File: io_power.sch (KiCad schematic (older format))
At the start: 30 parts, among them J7 Conn_02x03_Odd_Even, U11 TPS7A7100, U12 TPS7A7100, U13 ADS1115IDGS, U5 TCA6424A, U6 TPS7A7100

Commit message: sch: List LCSC P/N for each component
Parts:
- C22, C23, C24, C25, C26, C27, C31, C32, C33: LCSC P/N (none) -> C1591; MFR P/N (none) -> CL10B104KB8NNNC
- C28, C29, C30: LCSC P/N (none) -> C19702; MFR P/N (none) -> CL10A106KP8NNNC
- J7: LCSC P/N (none) -> C65114; MFR P/N (none) -> C65114
- R21, R22, R23: LCSC P/N (none) -> C115324; MFR P/N (none) -> RS-03K1002FT
- R24, R25, R26: LCSC P/N (none) -> C327826; MFR P/N (none) -> MR06X1003FTL
- R27, R28, R29: LCSC P/N (none) -> C413703; MFR P/N (none) -> ERJPB3B3002V
- R30, R31, R32: LCSC P/N (none) -> C191225; MFR P/N (none) -> ERJPB3B2002V
- U11, U12, U6: LCSC P/N (none) -> C129327; MFR P/N (none) -> TPS7A7100RGTR
- U13: LCSC P/N (none) -> C37593; MFR P/N (none) -> ADS1115IDGSR
- U5: LCSC P/N (none) -> C80692; MFR P/N (none) -> TCA6424ARGJR
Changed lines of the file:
@@
 F 2 "antboard:VQFN-16-1EP_3x3mm_P0.5mm_EP1.6x1.6mm_ThermalVias" H 7650 1100 50  0001 C CNN
 F 3 "https://www.ti.com/lit/ds/symlink/tps7a7100.pdf" H 7650 1100 50  0001 C CNN
+F 4 "C129327" H 7650 1100 50  0001 C CNN "LCSC P/N"
+F 5 "TPS7A7100RGTR" H 7650 1100 50  0001 C CNN "MFR P/N"
 	1    7650 1100
 	1    0    0    -1
@@
 F 2 "Capacitor_SMD:C_0603_1608Metric" H 8650 1400 50  0001 C CNN
 F 3 "~" H 8650 1400 50  0001 C CNN
+F 4 "C1591" H 8650 1400 50  0001 C CNN "LCSC P/N"
+F 5 "CL10B104KB8NNNC" H 8650 1400 50  0001 C CNN "MFR P/N"
 	1    8650 1400
 	-1   0    0    -1
@@
 F 2 "Resistor_SMD:R_0603_1608Metric" H 9000 1650 50  0001 C CNN
 F 3 "~" H 9000 1650 50  0001 C CNN
+F 4 "C327826" H 9000 1650 50  0001 C CNN "LCSC P/N"
+F 5 "MR06X1003FTL" H 9000 1650 50  0001 C CNN "MFR P/N"
 	1    9000 1650
 	1    0    0    -1
@@
 F 2 "antboard:VQFN-16-1EP_3x3mm_P0.5mm_EP1.6x1.6mm_ThermalVias" H 7650 2850 50  0001 C CNN
 F 3 "https://www.ti.com/lit/ds/symlink/tps7a7100.pdf" H 7650 2850 50  0001 C CNN
+F 4 "C129327" H 7650 2850 50  0001 C CNN "LCSC P/N"
+F 5 "TPS7A7100RGTR" H 7650 2850 50  0001 C CNN "MFR P/N"
 	1    7650 2850
 	1    0    0    -1
@@
 F 2 "Capacitor_SMD:C_0603_1608Metric" H 8650 3150 50  0001 C CNN
 F 3 "~" H 8650 3150 50  0001 C CNN
+F 4 "C1591" H 8650 3150 50  0001 C CNN "LCSC P/N"
+F 5 "CL10B104KB8NNNC" H 8650 3150 50  0001 C CNN "MFR P/N"
 	1    8650 3150
 	-1   0    0    -1
@@
 F 2 "Resistor_SMD:R_0603_1608Metric" H 9000 3400 50  0001 C CNN
 F 3 "~" H 9000 3400 50  0001 C CNN
+F 4 "C327826" H 9000 3400 50  0001 C CNN "LCSC P/N"
+F 5 "MR06X1003FTL" H 9000 3400 50  0001 C CNN "MFR P/N"
 	1    9000 3400
 	1    0    0    -1
@@
 F 2 "antboard:VQFN-16-1EP_3x3mm_P0.5mm_EP1.6x1.6mm_ThermalVias" H 7650 4600 50  0001 C CNN
 F 3 "https://www.ti.com/lit/ds/symlink/tps7a7100.pdf" H 7650 4600 50  0001 C CNN
+F 4 "C129327" H 7650 4600 50  0001 C CNN "LCSC P/N"
+F 5 "TPS7A7100RGTR" H 7650 4600 50  0001 C CNN "MFR P/N"
 	1    7650 4600
 	1    0    0    -1
@@
 F 2 "Capacitor_SMD:C_0603_1608Metric" H 8650 4900 50  0001 C CNN
 F 3 "~" H 8650 4900 50  0001 C CNN
+F 4 "C1591" H 8650 4900 50  0001 C CNN "LCSC P/N"
+F 5 "CL10B104KB8NNNC" H 8650 4900 50  0001 C CNN "MFR P/N"
 	1    8650 4900
 	-1   0    0    -1
@@
 F 2 "Resistor_SMD:R_0603_1608Metric" H 9000 5150 50  0001 C CNN
 F 3 "~" H 9000 5150 50  0001 C CNN
+F 4 "C327826" H 9000 5150 50  0001 C CNN "LCSC P/N"
+F 5 "MR06X1003FTL" H 9000 5150 50  0001 C CNN "MFR P/N"
 	1    9000 5150
 	1    0    0    -1
@@
 F 2 "Capacitor_SMD:C_0603_1608Metric" H 7350 5700 50  0001 C CNN
 F 3 "~" H 7350 5700 50  0001 C CNN
+F 4 "C1591" H 7350 5700 50  0001 C CNN "LCSC P/N"
+F 5 "CL10B104KB8NNNC" H 7350 5700 50  0001 C CNN "MFR P/N"
 	1    7350 5700
 	-1   0    0    -1
@@
 F 2 "Capacitor_SMD:C_0603_1608Metric" H 7350 3950 50  0001 C CNN
 F 3 "~" H 7350 3950 50  0001 C CNN
+F 4 "C1591" H 7350 3950 50  0001 C CNN "LCSC P/N"
+F 5 "CL10B104KB8NNNC" H 7350 3950 50  0001 C CNN "MFR P/N"
 	1    7350 3950
 	-1   0    0    -1
@@
 F 2 "Capacitor_SMD:C_0603_1608Metric" H 7350 2200 50  0001 C CNN
 F 3 "~" H 7350 2200 50  0001 C CNN
+F 4 "C1591" H 7350 2200 50  0001 C CNN "LCSC P/N"
+F 5 "CL10B104KB8NNNC" H 7350 2200 50  0001 C CNN "MFR P/N"
 	1    7350 2200
 	-1   0    0    -1
@@
 F 2 "Resistor_SMD:R_0603_1608Metric" H 7000 2200 50  0001 C CNN
 F 3 "~" H 7000 2200 50  0001 C CNN
+F 4 "C115324" H 7000 2200 50  0001 C CNN "LCSC P/N"
+F 5 "RS-03K1002FT" H 7000 2200 50  0001 C CNN "MFR P/N"
 	1    7000 2200
 	1    0    0    -1
@@
 F 2 "Resistor_SMD:R_0603_1608Metric" H 7000 3950 50  0001 C CNN
 F 3 "~" H 7000 3950 50  0001 C CNN
+F 4 "C115324" H 7000 3950 50  0001 C CNN "LCSC P/N"
+F 5 "RS-03K1002FT" H 7000 3950 50  0001 C CNN "MFR P/N"
 	1    7000 3950
 	1    0    0    -1
@@
 F 2 "Resistor_SMD:R_0603_1608Metric" H 7000 5700 50  0001 C CNN
 F 3 "~" H 7000 5700 50  0001 C CNN
+F 4 "C115324" H 7000 5700 50  0001 C CNN "LCSC P/N"
+F 5 "RS-03K1002FT" H 7000 5700 50  0001 C CNN "MFR P/N"
 	1    7000 5700
 	1    0    0    -1
@@
 F 2 "Package_DFN_QFN:QFN-32-1EP_5x5mm_P0.5mm_EP3.1x3.1mm" H 3650 2350 50  0001 C CNN
 F 3 "" H 3650 2350 50  0001 C CNN
+F 4 "C80692" H 3650 2350 50  0001 C CNN "LCSC P/N"
+F 5 "TCA6424ARGJR" H 3650 2350 50  0001 C CNN "MFR P/N"
 	1    3650 2350
 	1    0    0    -1
@@
 F 2 "Capacitor_SMD:C_0603_1608Metric" H 9300 2200 50  0001 C CNN
 F 3 "~" H 9300 2200 50  0001 C CNN
+F 4 "C19702" H 9300 2200 50  0001 C CNN "LCSC P/N"
+F 5 "CL10A106KP8NNNC" H 9300 2200 50  0001 C CNN "MFR P/N"
 	1    9300 2200
 	-1   0    0    -1
@@
 F 2 "Capacitor_SMD:C_0603_1608Metric" H 9300 3950 50  0001 C CNN
 F 3 "~" H 9300 3950 50  0001 C CNN
+F 4 "C19702" H 9300 3950 50  0001 C CNN "LCSC P/N"
+F 5 "CL10A106KP8NNNC" H 9300 3950 50  0001 C CNN "MFR P/N"
 	1    9300 3950
 	-1   0    0    -1
@@
 F 2 "Capacitor_SMD:C_0603_1608Metric" H 9300 5700 50  0001 C CNN
 F 3 "~" H 9300 5700 50  0001 C CNN
+F 4 "C19702" H 9300 5700 50  0001 C CNN "LCSC P/N"
+F 5 "CL10A106KP8NNNC" H 9300 5700 50  0001 C CNN "MFR P/N"
 	1    9300 5700
 	-1   0    0    -1
@@
 F 2 "Capacitor_SMD:C_0603_1608Metric" H 2400 2400 50  0001 C CNN
 F 3 "~" H 2400 2400 50  0001 C CNN
+F 4 "C1591" H 2400 2400 50  0001 C CNN "LCSC P/N"
+F 5 "CL10B104KB8NNNC" H 2400 2400 50  0001 C CNN "MFR P/N"
 	1    2400 2400
 	-1   0    0    -1
@@
 F 2 "Capacitor_SMD:C_0603_1608Metric" H 2600 2400 50  0001 C CNN
 F 3 "~" H 2600 2400 50  0001 C CNN
+F 4 "C1591" H 2600 2400 50  0001 C CNN "LCSC P/N"
+F 5 "CL10B104KB8NNNC" H 2600 2400 50  0001 C CNN "MFR P/N"
 	1    2600 2400
 	1    0    0    -1
@@
 F 2 "Connector_PinHeader_2.54mm:PinHeader_2x03_P2.54mm_Vertical" H 10250 3650 50  0001 C CNN
 F 3 "~" H 10250 3650 50  0001 C CNN
+F 4 "C65114" H 10250 3650 50  0001 C CNN "LCSC P/N"
+F 5 "C65114" H 10250 3650 50  0001 C CNN "MFR P/N"
 	1    10250 3650
 	1    0    0    -1
@@
 F 2 "Resistor_SMD:R_0603_1608Metric" H 3550 6750 50  0001 C CNN
 F 3 "~" H 3550 6750 50  0001 C CNN
+F 4 "C191225" H 3550 6750 50  0001 C CNN "LCSC P/N"
+F 5 "ERJPB3B2002V" H 3550 6750 50  0001 C CNN "MFR P/N"
 	1    3550 6750
 	1    0    0    -1
@@
 F 2 "Resistor_SMD:R_0603_1608Metric" H 2850 6350 50  0001 C CNN
 F 3 "~" H 2850 6350 50  0001 C CNN
+F 4 "C413703" H 2850 6350 50  0001 C CNN "LCSC P/N"
+F 5 "ERJPB3B3002V" H 2850 6350 50  0001 C CNN "MFR P/N"
 	1    2850 6350
 	0    1    1    0
@@
 F 2 "Capacitor_SMD:C_0603_1608Metric" H 3800 5850 50  0001 C CNN
 F 3 "~" H 3800 5850 50  0001 C CNN
+F 4 "C1591" H 3800 5850 50  0001 C CNN "LCSC P/N"
+F 5 "CL10B104KB8NNNC" H 3800 5850 50  0001 C CNN "MFR P/N"
 	1    3800 5850
 	0    -1   -1   0
@@
 F 2 "Package_SO:TSSOP-10_3x3mm_P0.5mm" H 4050 5950 50  0001 C CNN
 F 3 "http://www.ti.com/lit/ds/symlink/ads1113.pdf" H 4000 5550 50  0001 C CNN
+F 4 "C37593" H 4050 6450 50  0001 C CNN "LCSC P/N"
+F 5 "ADS1115IDGSR" H 4050 6450 50  0001 C CNN "MFR P/N"
 	1    4050 6450
 	1    0    0    -1
@@
 F 2 "Resistor_SMD:R_0603_1608Metric" H 3300 6750 50  0001 C CNN
 F 3 "~" H 3300 6750 50  0001 C CNN
+F 4 "C191225" H 3300 6750 50  0001 C CNN "LCSC P/N"
+F 5 "ERJPB3B2002V" H 3300 6750 50  0001 C CNN "MFR P/N"
 	1    3300 6750
 	1    0    0    -1
@@
 F 2 "Resistor_SMD:R_0603_1608Metric" H 3050 6750 50  0001 C CNN
 F 3 "~" H 3050 6750 50  0001 C CNN
+F 4 "C191225" H 3050 6750 50  0001 C CNN "LCSC P/N"
+F 5 "ERJPB3B2002V" H 3050 6750 50  0001 C CNN "MFR P/N"
 	1    3050 6750
 	1    0    0    -1
@@
 F 2 "Resistor_SMD:R_0603_1608Metric" H 2850 6450 50  0001 C CNN
 F 3 "~" H 2850 6450 50  0001 C CNN
+F 4 "C413703" H 2850 6450 50  0001 C CNN "LCSC P/N"
+F 5 "ERJPB3B3002V" H 2850 6450 50  0001 C CNN "MFR P/N"
 	1    2850 6450
 	0    1    1    0
@@
 F 2 "Resistor_SMD:R_0603_1608Metric" H 2850 6550 50  0001 C CNN
 F 3 "~" H 2850 6550 50  0001 C CNN
+F 4 "C413703" H 2850 6550 50  0001 C CNN "LCSC P/N"
+F 5 "ERJPB3B3002V" H 2850 6550 50  0001 C CNN "MFR P/N"
 	1    2850 6550
 	0    1    1    0

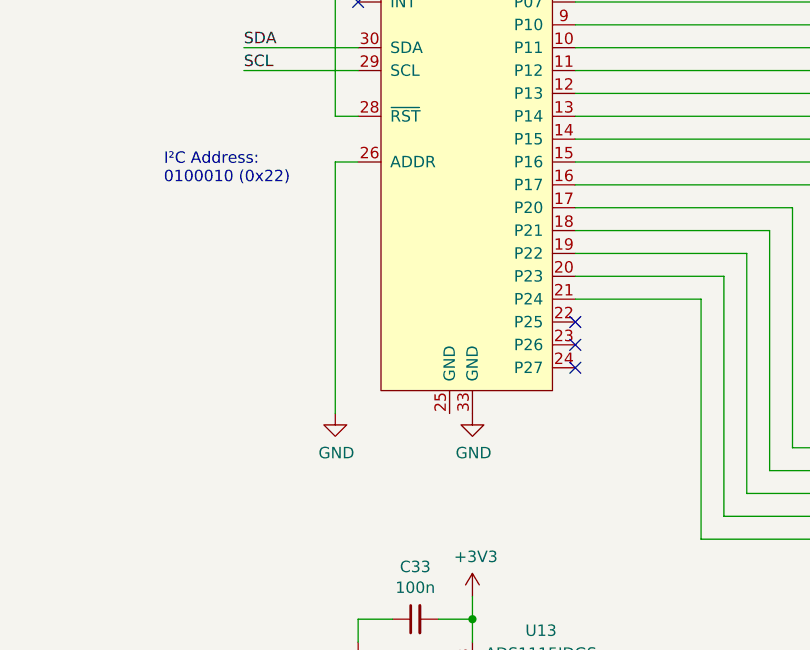
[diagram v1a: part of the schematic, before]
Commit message: sch, pcb: Connect TCA epad to GND
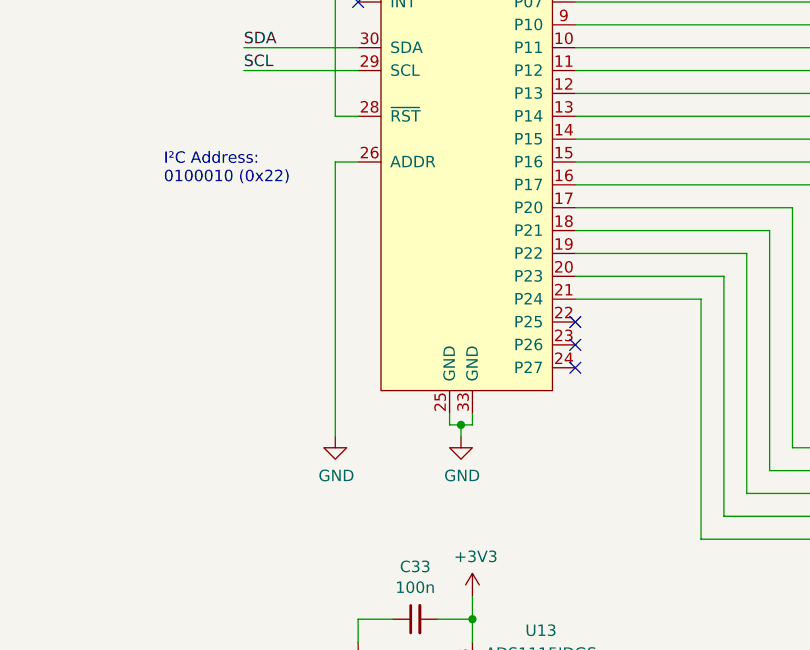
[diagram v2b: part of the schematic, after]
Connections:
- net GND: now also U5.25 (GND)
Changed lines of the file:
@@
 Wire Wire Line
 	4050 2200 4100 2200
-$Comp
-L power:GND #PWR?
-U 1 1 5DE8B0E0
-P 4050 4950
-AR Path="/5DE8B0E0" Ref="#PWR?"  Part="1"
-AR Path="/5DF7E971/5DE8B0E0" Ref="#PWR?"  Part="1"
-AR Path="/5DFC2583/5DE8B0E0" Ref="#PWR?"  Part="1"
-AR Path="/5EA8F1AB/5DE8B0E0" Ref="#PWR028"  Part="1"
-F 0 "#PWR028" H 4050 4700 50  0001 C CNN
-F 1 "GND" H 4055 4777 50  0000 C CNN
-F 2 "" H 4050 4950 50  0001 C CNN
-F 3 "" H 4050 4950 50  0001 C CNN
-	1    4050 4950
-	1    0    0    -1
-$EndComp
 Wire Wire Line
 	3550 3650 3450 3650
@@
 Wire Wire Line
 	3550 3850 3450 3850
-$Comp
-L power:GND #PWR?
-U 1 1 5DE9ACDD
-P 3450 4950
-AR Path="/5DE9ACDD" Ref="#PWR?"  Part="1"
-AR Path="/5DF7E971/5DE9ACDD" Ref="#PWR?"  Part="1"
-AR Path="/5DFC2583/5DE9ACDD" Ref="#PWR?"  Part="1"
-AR Path="/5EA8F1AB/5DE9ACDD" Ref="#PWR011"  Part="1"
-F 0 "#PWR011" H 3450 4700 50  0001 C CNN
-F 1 "GND" H 3455 4777 50  0000 C CNN
-F 2 "" H 3450 4950 50  0001 C CNN
-F 3 "" H 3450 4950 50  0001 C CNN
-	1    3450 4950
-	1    0    0    -1
-$EndComp
 $Comp
 L power:+3V3 #PWR010
@@
 	1    0    0    -1
 $EndComp
-Wire Wire Line
-	3450 3850 3450 4950
 $Comp
 L antboard:TCA6424A U5
@@
 Text HLabel 1100 1200 0    50   Output ~ 0
 DRDY
+Wire Wire Line
+	3950 4950 3950 5000
+Wire Wire Line
+	4050 5000 4050 4950
+Wire Wire Line
+	3950 5000 4000 5000
+Wire Wire Line
+	4000 5000 4050 5000
+Connection ~ 4000 5000
+$Comp
+L power:GND #PWR?
+U 1 1 5DE8B0E0
+P 4000 5050
+AR Path="/5DE8B0E0" Ref="#PWR?"  Part="1"
+AR Path="/5DF7E971/5DE8B0E0" Ref="#PWR?"  Part="1"
+AR Path="/5DFC2583/5DE8B0E0" Ref="#PWR?"  Part="1"
+AR Path="/5EA8F1AB/5DE8B0E0" Ref="#PWR028"  Part="1"
+F 0 "#PWR028" H 4000 4800 50  0001 C CNN
+F 1 "GND" H 4005 4877 50  0000 C CNN
+F 2 "" H 4000 5050 50  0001 C CNN
+F 3 "" H 4000 5050 50  0001 C CNN
+	1    4000 5050
+	1    0    0    -1
+$EndComp
+Wire Wire Line
+	4000 5000 4000 5050
+$Comp
+L power:GND #PWR?
+U 1 1 5DE9ACDD
+P 3450 5050
+AR Path="/5DE9ACDD" Ref="#PWR?"  Part="1"
+AR Path="/5DF7E971/5DE9ACDD" Ref="#PWR?"  Part="1"
+AR Path="/5DFC2583/5DE9ACDD" Ref="#PWR?"  Part="1"
+AR Path="/5EA8F1AB/5DE9ACDD" Ref="#PWR011"  Part="1"
+F 0 "#PWR011" H 3450 4800 50  0001 C CNN
+F 1 "GND" H 3455 4877 50  0000 C CNN
+F 2 "" H 3450 5050 50  0001 C CNN
+F 3 "" H 3450 5050 50  0001 C CNN
+	1    3450 5050
+	1    0    0    -1
+$EndComp
+Wire Wire Line
+	3450 3850 3450 5050
 $EndSCHEMATC
